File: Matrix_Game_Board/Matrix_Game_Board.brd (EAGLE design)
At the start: 162 x 64 mm, 48 parts, among them J1 AVR_SPI_PRG_6NS, J2 AVR_SPI_PRG_6NS, J3 AVR_SPI_PRG_6NS, J4 AVR_SPI_PRG_6NS

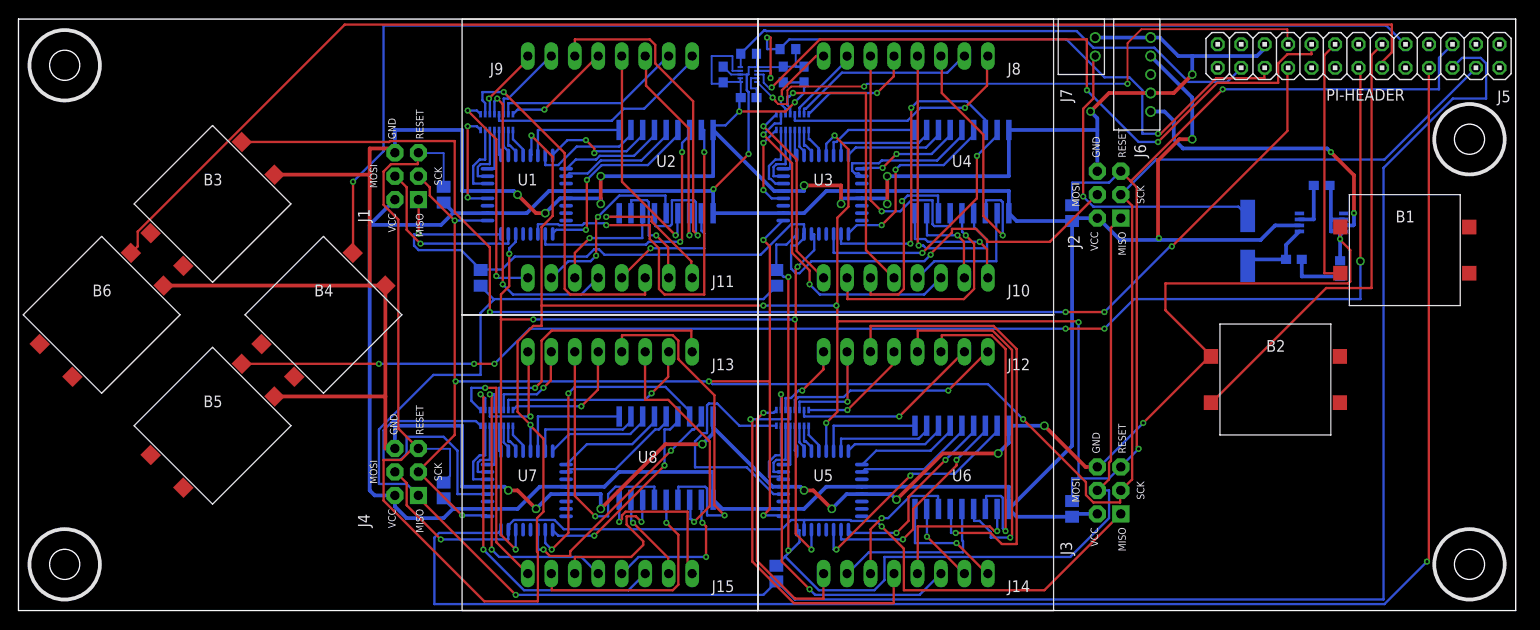
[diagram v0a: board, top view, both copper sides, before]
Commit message: Added start and select buttons to matrix board and moved accelerometer to the middle of the board
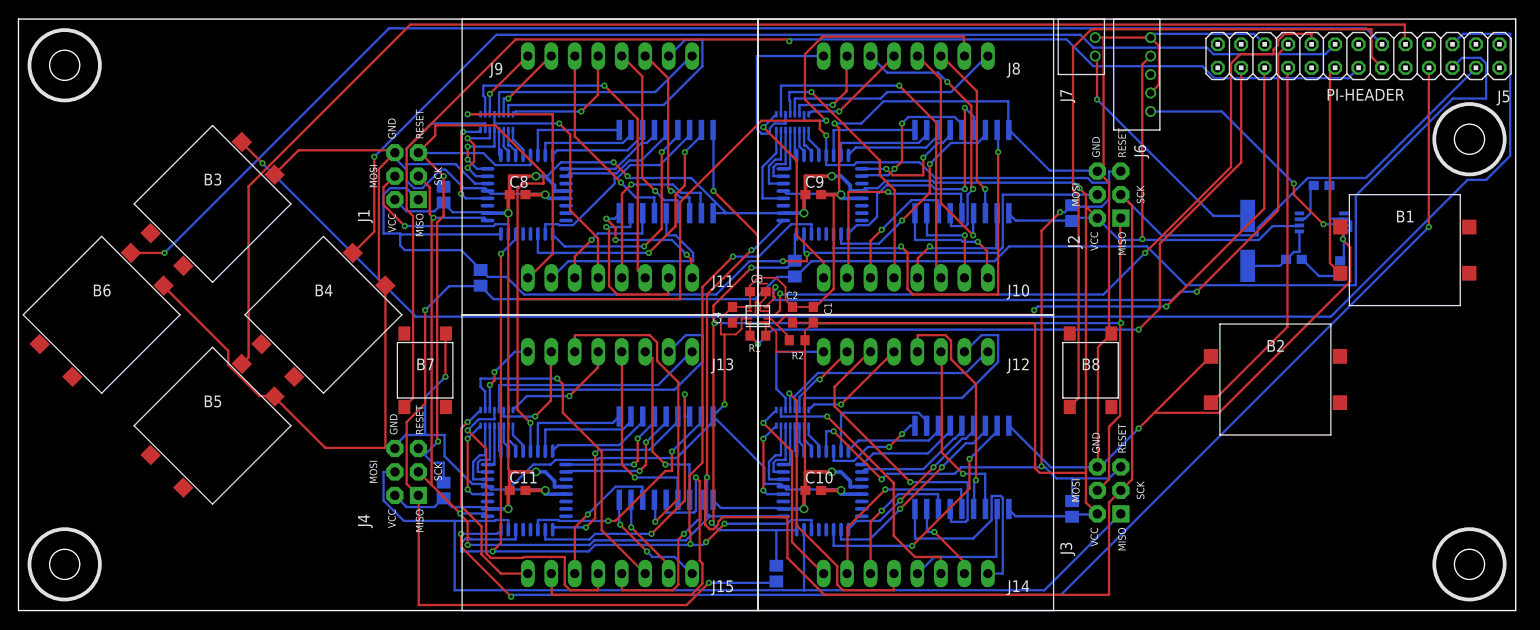
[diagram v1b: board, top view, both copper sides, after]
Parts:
- added C10, C11, C8, C9: (no value), resistor:C0603
- added U$24, U$26: SMDTACTILE, ScottSilver:SMDTACTILE
- moved R2 31.5 mm to (82.2, 29.2), flipped to the top, turned to 180 degrees
- moved R1 30.5 mm to (78.0, 29.8), flipped to the top, turned to 0 degrees
- moved C1 26.0 mm to (84.0, 32.0), flipped to the top, turned to 90 degrees
- moved C2 26.0 mm to (81.8, 32.0), flipped to the top, turned to 90 degrees
- moved C4 26.0 mm to (75.2, 32.0), flipped to the top, turned to 90 degrees
- moved U$23 26.0 mm to (78.0, 32.0), flipped to the top, turned to 180 degrees
- moved C3 21.0 mm to (78.0, 34.5), flipped to the top, turned to 180 degrees
- moved R9 2.24 mm to (82.0, 37.0)
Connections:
- new net SELECT: PI-HEADER.15, U$26.1
- new net START: PI-HEADER.13, U$24.1
- net A: now also PI-HEADER.7; no longer PI-HEADER.16
- net B: now also PI-HEADER.11; no longer PI-HEADER.12
- net DOWN: now also PI-HEADER.18; no longer PI-HEADER.13
- net GND: now also C10.2, C11.2, C8.2, C9.2, U$24.4, U$26.4
- net LEFT: now also PI-HEADER.16; no longer PI-HEADER.15
- net RESET: no longer PI-HEADER.22
- net RIGHT: now also PI-HEADER.12; no longer PI-HEADER.18
- net UP: now also PI-HEADER.22; no longer PI-HEADER.7
- net VCC: now also C10.1, C11.1, C8.1, C9.1
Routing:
- net START: track 0.00 -> 139.0 mm, vias 0 -> 1
- net RESET: track 347.1 -> 268.4 mm, vias 9 -> 8
- net SELECT: track 0.00 -> 77.3 mm
- net MOSI: track 177.6 -> 146.7 mm, vias 1 -> 3
- net MISO: track 245.7 -> 215.9 mm, vias 1 -> 2
- net VCC: track 322.6 -> 351.0 mm, vias 4 -> 12
- net UP: track 144.5 -> 172.2 mm, vias 4 -> 1
- net SCK: track 247.2 -> 273.6 mm, vias 7 -> 5
- net N$4: track 45.7 -> 21.8 mm
- net N$95: track 33.0 -> 9.84 mm, vias 0 -> 2
- net GND: track 434.9 -> 456.6 mm, vias 23 -> 10
- net SS: track 107.7 -> 128.0 mm
- net N$106: track 51.0 -> 32.8 mm
- net SDA: track 59.6 -> 77.6 mm, vias 0 -> 2
- net N$75: track 38.6 -> 21.3 mm
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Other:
- board text added: "B7"
- board text added: "B8"

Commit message: Corrected some net names on Gamer PCB
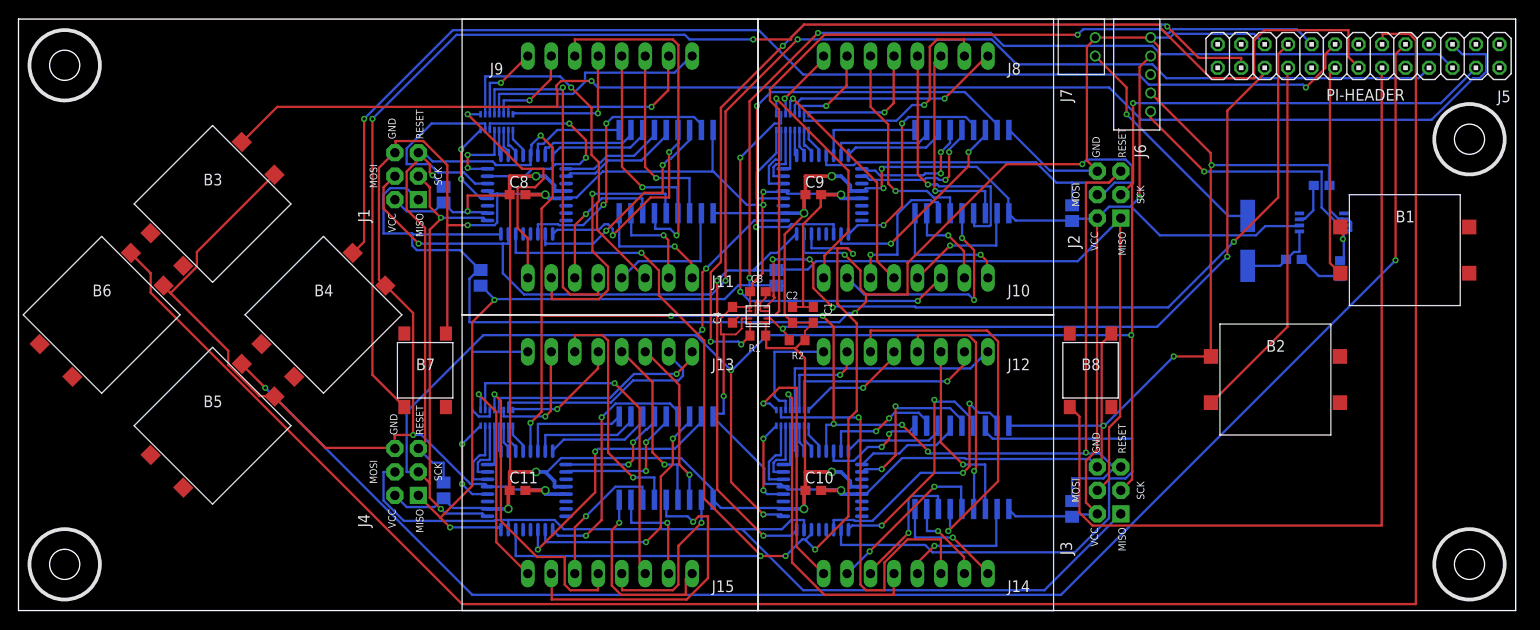
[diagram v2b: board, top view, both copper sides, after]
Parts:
- removed R9: Bypass, resistor:R0805
- moved R4 32.0 mm to (80.0, 36.0)
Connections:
- removed net MOSI1: J1.4, U$9.PB3
- net MISO: now also U$11.PB4; no longer R9.2
- net MISO2/MOSI3: no longer R9.1
- net MOSI: now also J1.4, U$9.PB3; no longer U$11.PB4
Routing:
- net LEFT: track 146.2 -> 222.1 mm, vias 1 -> 0
- net MISO: track 215.9 -> 171.2 mm, vias 2 -> 4
- net VCC: track 351.0 -> 309.5 mm, vias 12 -> 11
- net N$125: track 22.1 -> 60.1 mm, vias 2 -> 0
- net MISO1/MOSI2: track 111.2 -> 137.3 mm, vias 2 -> 3
- net UP: track 172.2 -> 148.7 mm
- net DOWN: track 154.1 -> 174.0 mm, vias 0 -> 2
- net MOSI1: track 19.2 -> 0.00 mm, vias 1 -> 0
- net SELECT: track 77.3 -> 94.7 mm
- net SDA: track 77.6 -> 94.6 mm, vias 2 -> 4
- net N$4: track 21.8 -> 38.3 mm
- net START: track 139.0 -> 154.7 mm, vias 1 -> 2
- net N$27: track 9.60 -> 25.2 mm
- net N$117: track 29.4 -> 44.1 mm
- net RESET: track 268.4 -> 254.4 mm, vias 8 -> 9
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
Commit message: Corrected some more net names on Gamer PCB
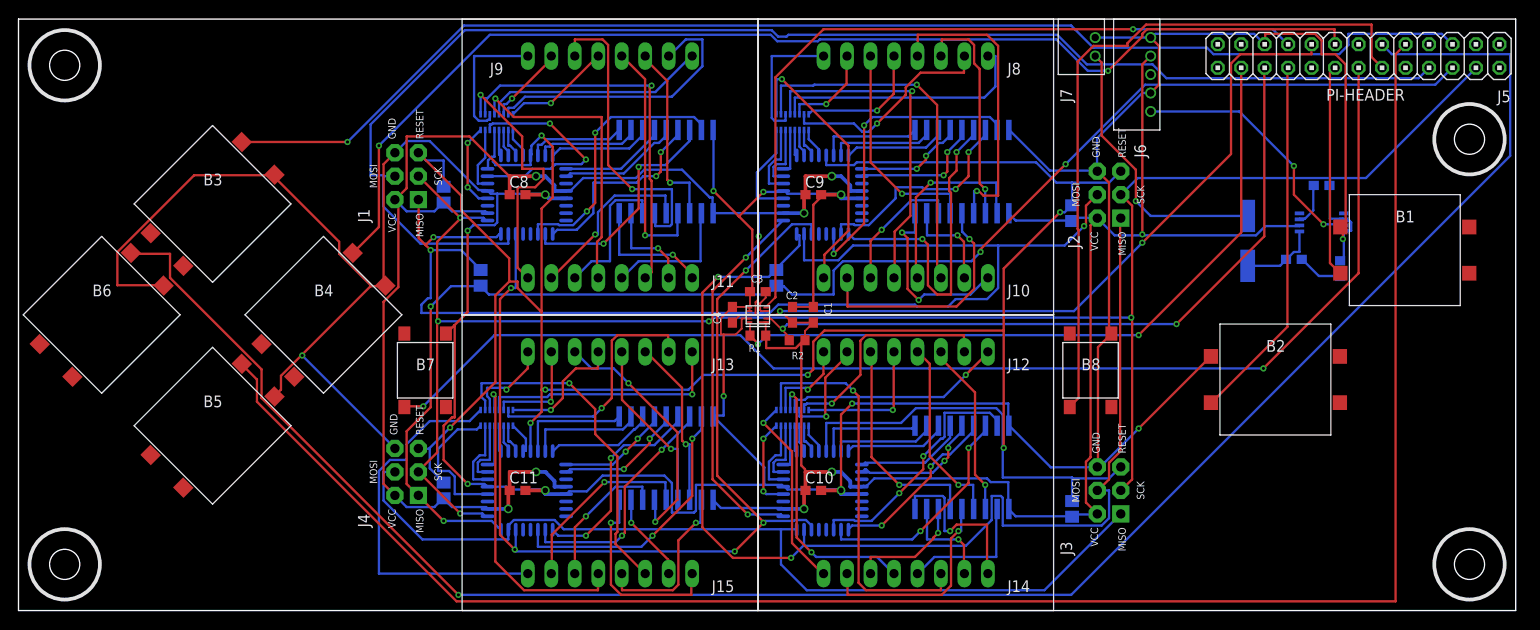
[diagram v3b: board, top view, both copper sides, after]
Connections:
- net MISO2/MOSI3: now also U$15.PB3; no longer U$15.PB4
- net MISO3/MOSI4: now also U$15.PB4; no longer U$15.PB3
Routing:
- net N$125: track 60.1 -> 24.3 mm, vias 0 -> 2
- net GND: track 450.4 -> 479.1 mm
- net DOWN: track 174.0 -> 197.6 mm, vias 2 -> 0
- net SS: track 135.2 -> 113.2 mm
- net SCK: track 263.7 -> 242.0 mm, vias 8 -> 7
- net START: track 154.7 -> 134.5 mm
- net N$85: track 23.5 -> 41.9 mm, vias 1 -> 0
- net N$60: track 51.4 -> 33.2 mm
- net SELECT: track 94.7 -> 76.6 mm
- net N$106: track 41.9 -> 23.8 mm
- net SDA: track 94.6 -> 77.9 mm, vias 4 -> 2
- net N$25: track 21.6 -> 7.18 mm
- net MISO: track 171.2 -> 157.1 mm
- net VCC: track 309.5 -> 322.9 mm, vias 11 -> 9
- net N$74: track 34.3 -> 20.9 mm
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
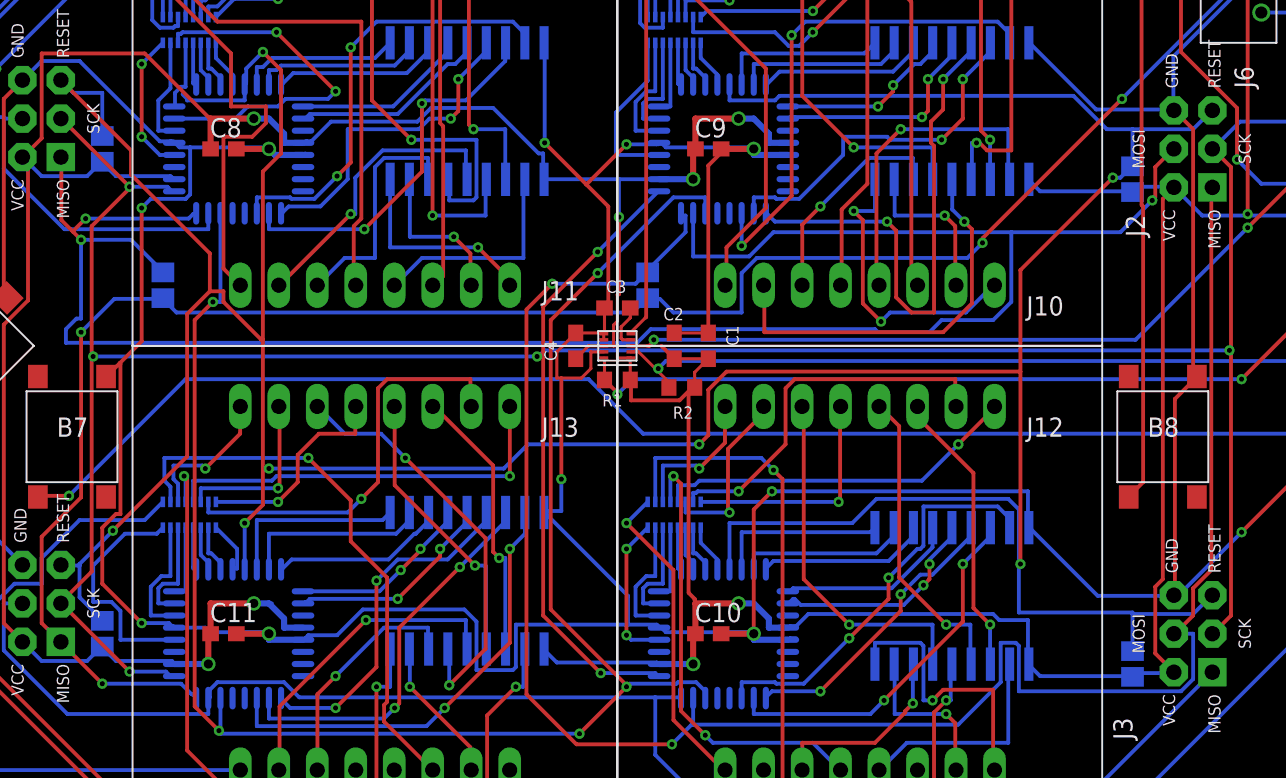
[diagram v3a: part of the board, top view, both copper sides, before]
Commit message: Changed resistors to 0603 on gamer PCB
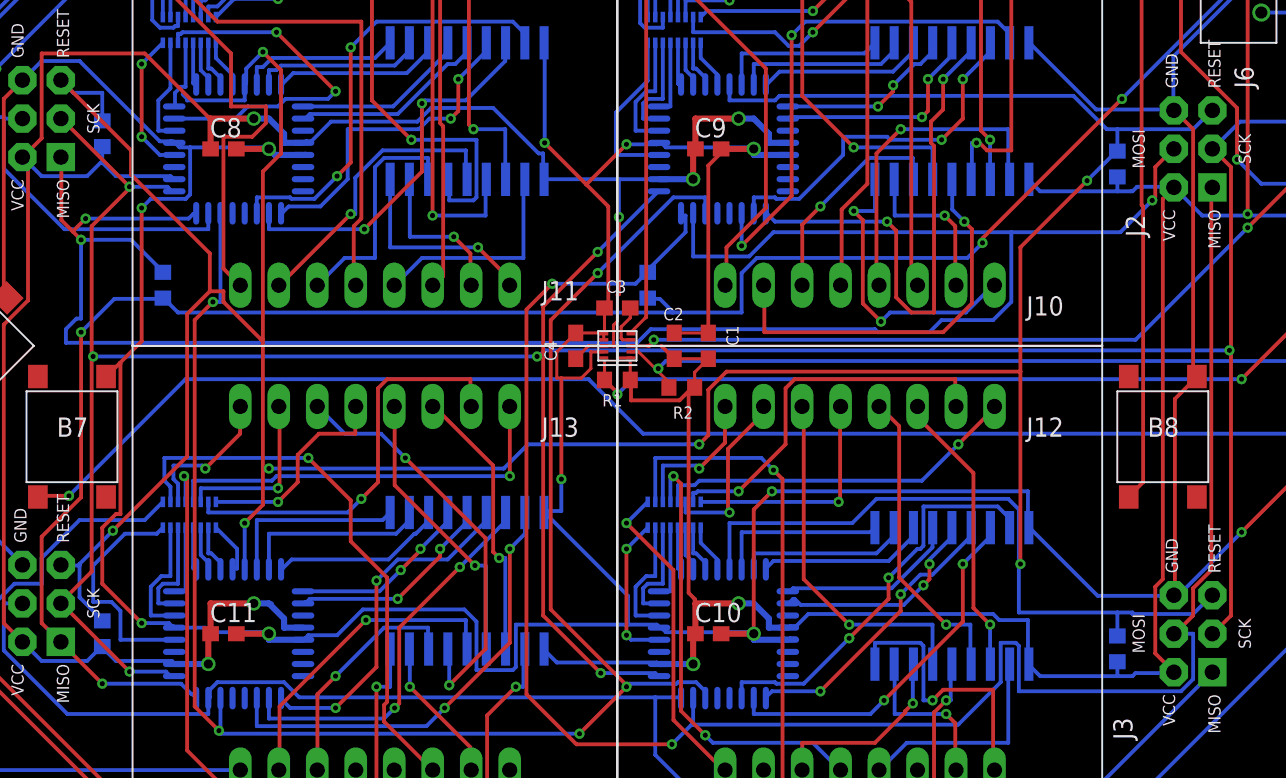
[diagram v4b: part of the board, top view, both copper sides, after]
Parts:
- removed R10: 100k, resistor:R0805
- added R9: 100K, resistor:R0603
- R3, R4: device resistor:R0805 -> resistor:R0603
- R5, R6, R8: value 100k -> 100K; device resistor:R0805 -> resistor:R0603
- moved R8 67.0 mm to (111.0, 12.0)
- moved R5 1.41 mm to (111.0, 44.0)
- moved R6 1.00 mm to (44.0, 46.0)
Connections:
- net RESET: now also R9.1; no longer R10.1
- net VCC: now also R9.2; no longer R10.2
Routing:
- net VCC: track 322.9 -> 325.7 mm
- net RESET: track 266.9 -> 264.3 mm
- net MISO: track 157.1 -> 158.4 mm

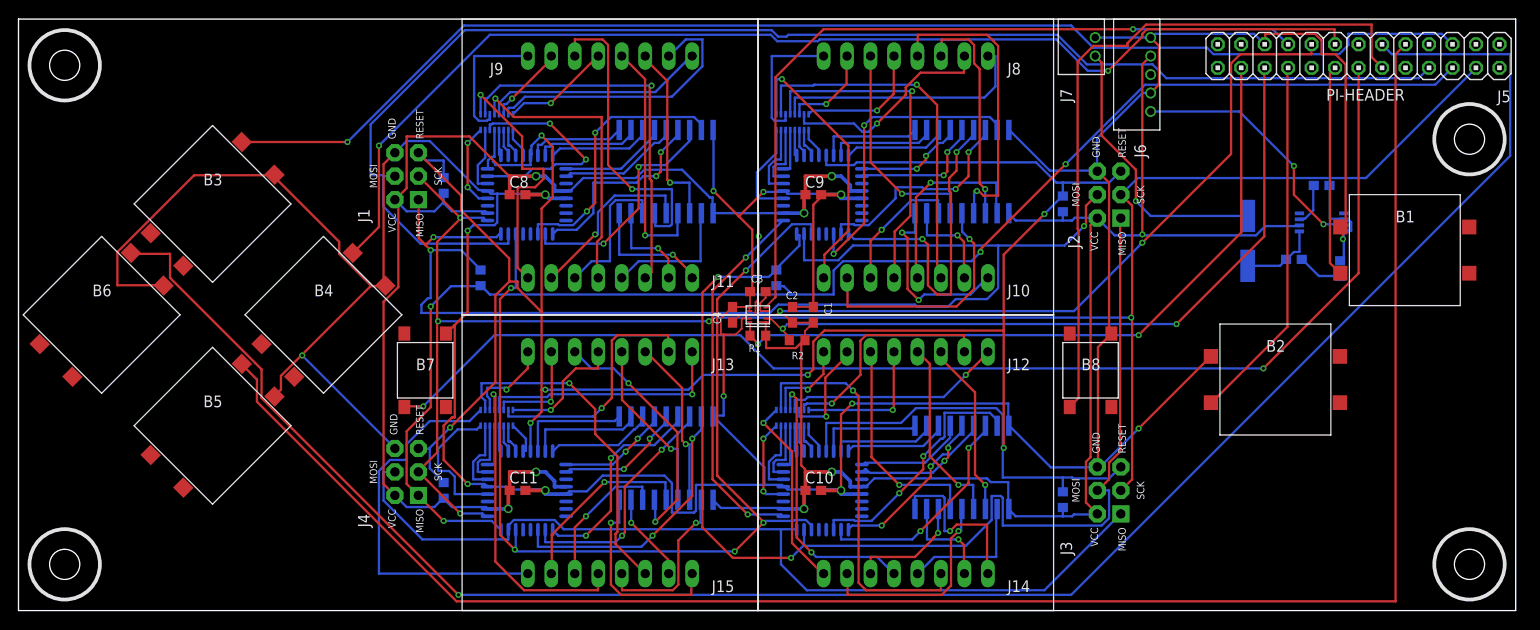
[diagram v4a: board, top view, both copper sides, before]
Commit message: Moved start and select, moved pi header down to make screws in 2x6in square
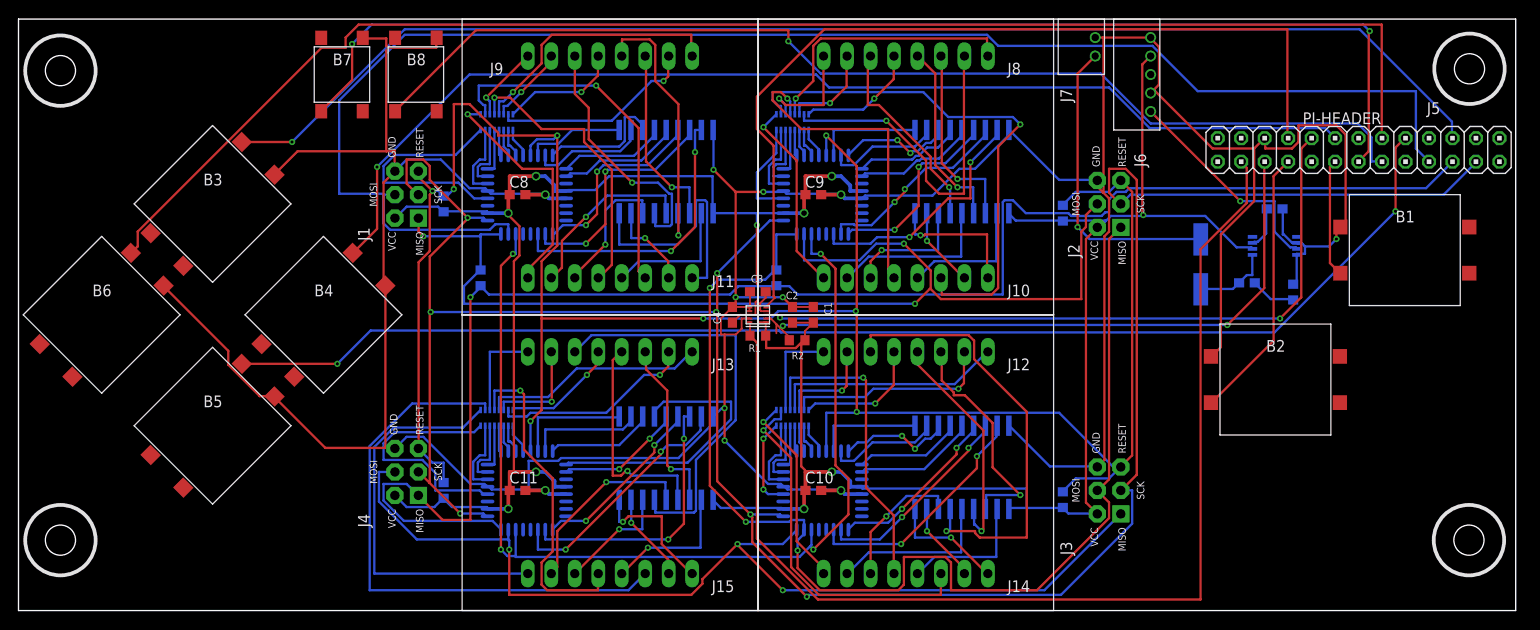
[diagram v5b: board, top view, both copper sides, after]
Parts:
- moved U$26 79.7 mm to (41.0, 58.0)
- moved U$24 33.2 mm to (33.0, 58.0)
- moved PI-HEADER 10.2 mm to (143.0, 49.8)
- moved C6 5.68 mm to (130.9, 35.5)
- moved C7 5.68 mm to (133.9, 43.5)
- moved R7 5.68 mm to (135.9, 34.5)
- moved U$25 5.68 mm to (133.9, 39.5)
- moved C5 5.68 mm to (125.9, 37.5)
- moved J1 2.00 mm to (40.0, 45.0)
- moved R6 2.00 mm to (44.0, 44.0)
- moved J2 1.00 mm to (116.0, 44.0)
- moved R5 1.00 mm to (111.0, 43.0)
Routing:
- net DOWN: track 197.6 -> 140.2 mm, vias 0 -> 2
- net LEFT: track 212.9 -> 159.4 mm, vias 1 -> 0
- net SDA: track 77.9 -> 124.2 mm, vias 2 -> 0
- net SELECT: track 76.6 -> 118.6 mm, vias 0 -> 1
- net VCC: track 325.7 -> 293.9 mm, vias 9 -> 10
- net GND: track 479.1 -> 448.3 mm, vias 13 -> 11
- net N$106: track 23.8 -> 48.8 mm
- net N$84: track 36.7 -> 61.3 mm, vias 1 -> 0
- net SCK: track 242.0 -> 265.8 mm
- net N$89: track 12.2 -> 31.1 mm, vias 2 -> 0
- net N$51: track 39.8 -> 58.2 mm
- net MISO1/MOSI2: track 135.5 -> 118.4 mm
- net N$73: track 27.8 -> 44.8 mm, vias 2 -> 0
- net N$27: track 24.1 -> 7.17 mm, vias 2 -> 0
- net N$26: track 9.43 -> 25.9 mm, vias 2 -> 0
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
